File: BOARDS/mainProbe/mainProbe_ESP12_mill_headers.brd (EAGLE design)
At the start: 34 x 54.6 mm, 18 parts

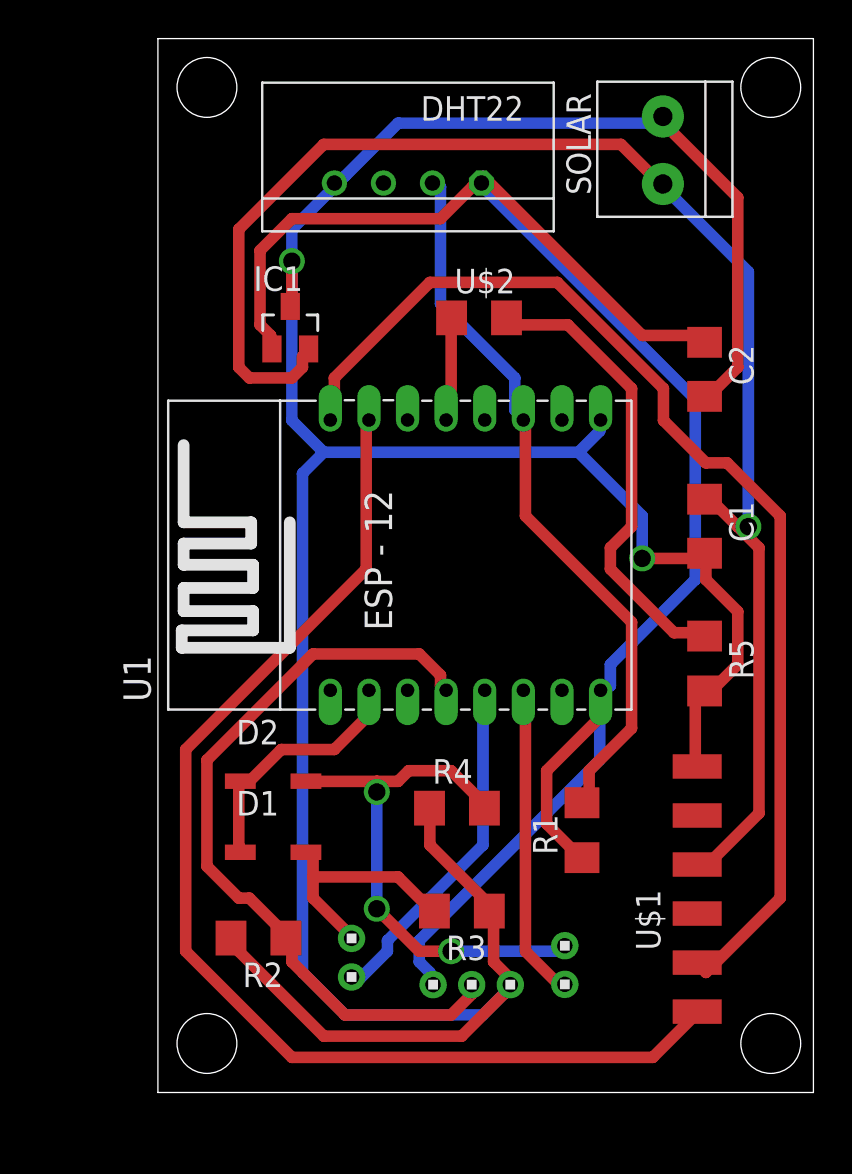
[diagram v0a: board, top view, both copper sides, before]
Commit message: placa com headers thanks to FS
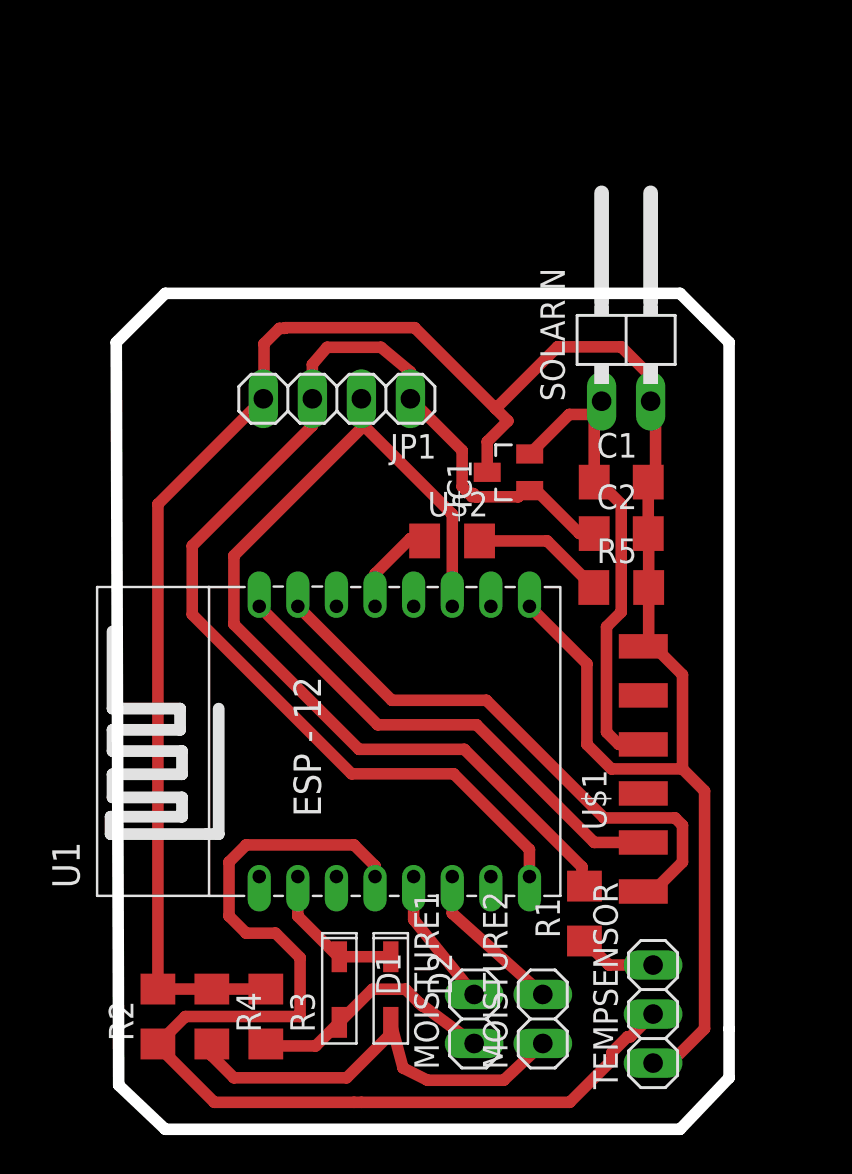
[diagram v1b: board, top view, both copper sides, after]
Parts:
- removed DHT22: (no value), RHT03_DHT-22_AM2302:RHT03_DHT-22
- removed SOLAR: TERM-1X02-ADAFRUIT, fab:3.5MMTERM
- added JP1: (no value), pinhead:1X04
- added SOLARIN: (no value), pinhead:1X02/90
- MOISTURE1, MOISTURE2: value 1X2 -> (none); device headers(2mm):1X2 -> pinhead:1X02
- TEMPSENSOR: value 1X3 -> (none); device headers(2mm):1X3 -> pinhead:1X03
- moved R4 16.7 mm to (5.33, 6.48), turned to 270 degrees
- moved IC1 13.6 mm to (20.7, 34.7), turned to 90 degrees
- moved D2 12.4 mm to (14.6, 7.87), turned to 270 degrees
- moved U$2 11.6 mm to (17.8, 31.1)
- moved R3 11.5 mm to (8.13, 6.48), turned to 270 degrees
- moved U1 10.3 mm to (13.6, 20.8)
- moved C2 9.54 mm to (26.5, 31.5), turned to 0 degrees
- moved TEMPSENSOR 9.52 mm to (28.2, 6.60), turned to 90 degrees
- moved D1 7.90 mm to (11.9, 7.87), turned to 270 degrees
- moved MOISTURE1 7.10 mm to (18.9, 6.35)
- moved U$1 6.82 mm to (27.7, 19.3)
- moved R2 6.61 mm to (2.54, 6.48), turned to 90 degrees
- moved R5 5.84 mm to (26.5, 28.7), turned to 0 degrees
- moved C1 4.89 mm to (26.5, 34.2), turned to 0 degrees
- moved R1 4.32 mm to (24.6, 11.8)
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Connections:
- net 3.3V: now also JP1.1, JP1.3, TEMPSENSOR.3; no longer DHT22.VDD, TEMPSENSOR.1
- net GND: now also JP1.4, SOLARIN.2, TEMPSENSOR.1; no longer DHT22.GND, SOLAR.1, TEMPSENSOR.3
- net N$5: now also MOISTURE1.1; no longer MOISTURE1.2
- net N$7: now also MOISTURE2.1; no longer MOISTURE2.2
- net N$8: now also JP1.2; no longer DHT22.DATA
- net ONMOIST1: now also MOISTURE1.2; no longer MOISTURE1.1
- net ONMOIST2: now also MOISTURE2.2; no longer MOISTURE2.1
- net VIN: now also SOLARIN.1; no longer SOLAR.2
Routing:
- net VIN: track 78.8 -> 24.5 mm, vias 1 -> 0
- net GND: track 161.3 -> 122.6 mm, vias 2 -> 0
- net TX: track 59.3 -> 25.0 mm
- net RX: track 61.3 -> 29.2 mm
- net 3.3V: track 96.7 -> 64.9 mm
- net N$6: track 24.1 -> 6.92 mm
- net N$3: track 39.8 -> 56.7 mm
- net N$8: track 37.8 -> 50.4 mm
- net ONMOIST1: track 18.3 -> 7.22 mm
- net ONMOIST2: track 16.3 -> 8.20 mm
- net ADC: track 13.1 -> 7.74 mm
- net N$7: track 27.7 -> 23.2 mm, vias 3 -> 0
- net N$5: track 12.5 -> 13.3 mm
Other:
- board size 34 x 54.6 mm -> 31.8 x 43.3 mm
